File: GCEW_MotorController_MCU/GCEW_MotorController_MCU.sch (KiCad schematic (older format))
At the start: 4 parts, among them J1 Conn_02x03_Odd_Even, U1 ATMEGA328PB-AU

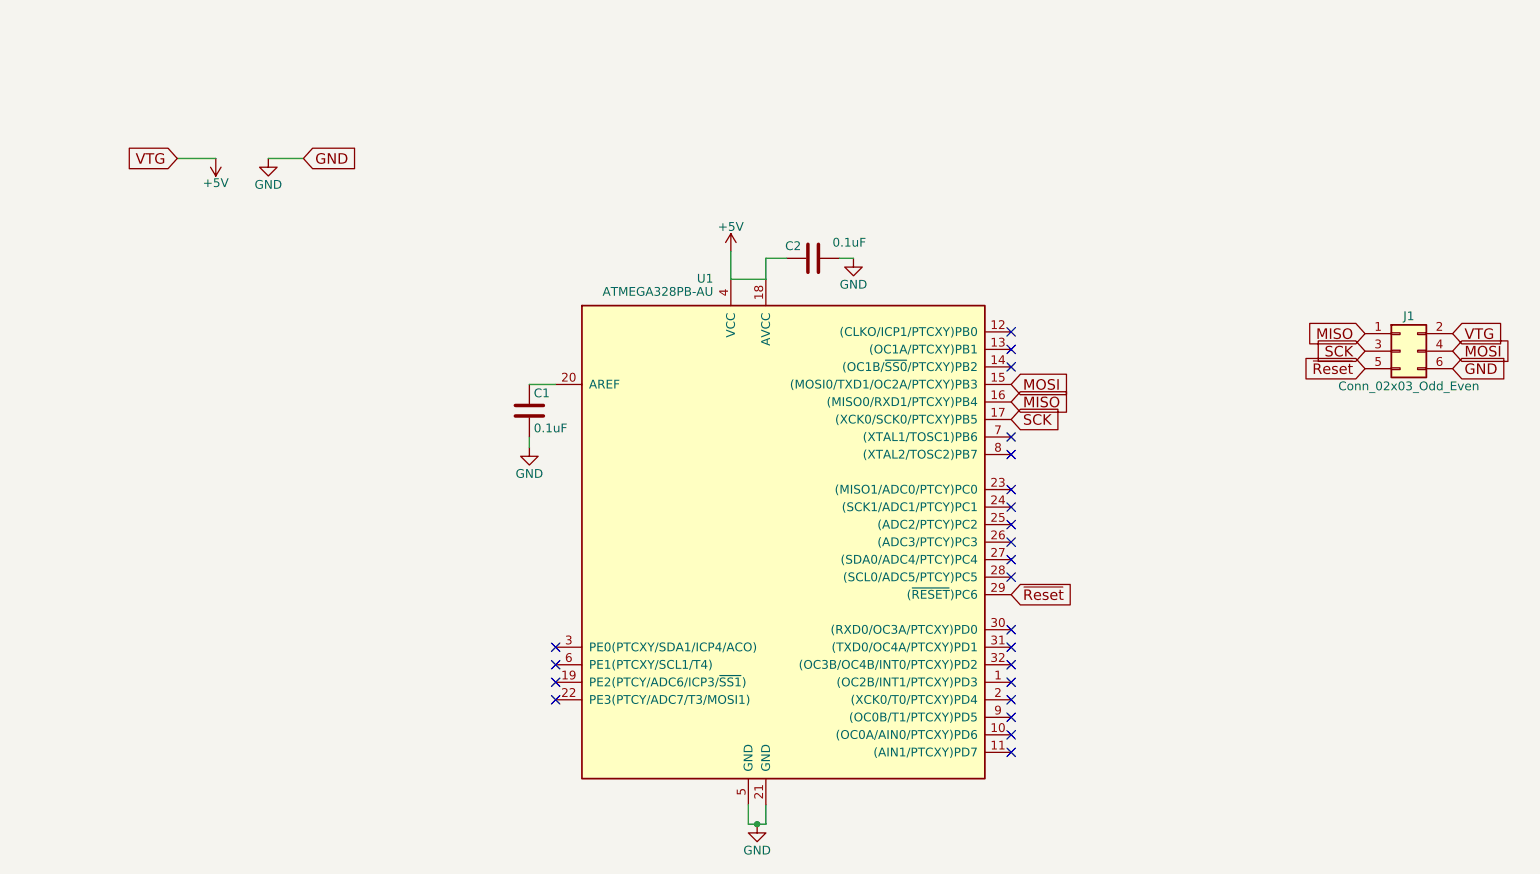
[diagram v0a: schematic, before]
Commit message: KiCAD Motor Controller MCU Schematic Update 1
Began KiCAD Schematic Design of Motor Controller MCU Board
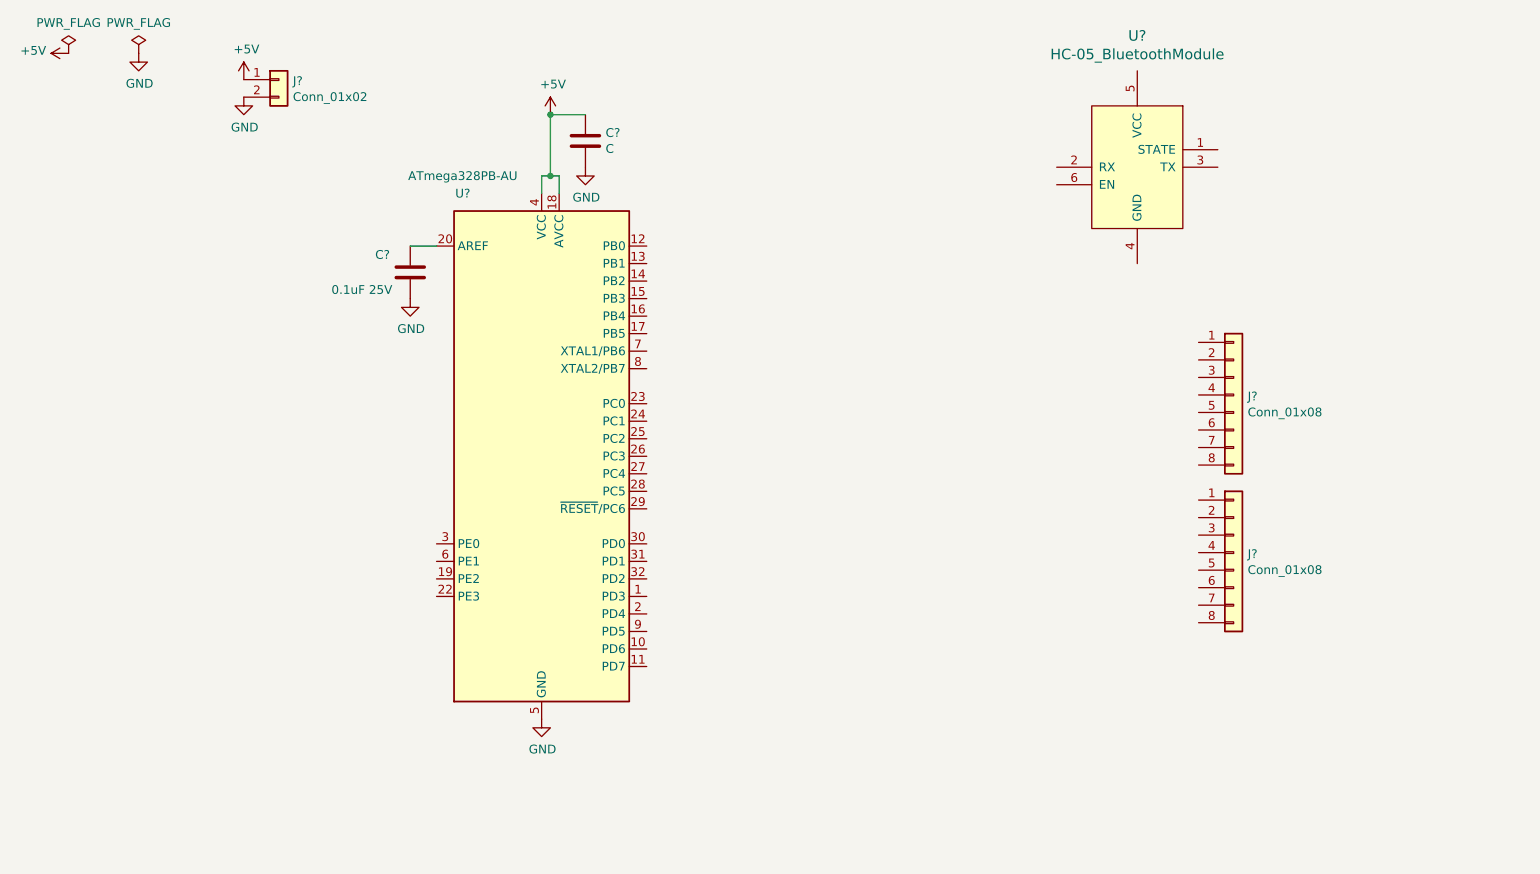
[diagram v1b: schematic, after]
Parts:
- removed C1, C2: 0.1uF, symbol C
- removed J1: Conn_02x03_Odd_Even, symbol Conn_02x03_Odd_Even
- removed U1: ATMEGA328PB-AU, Housings_QFP:TQFP-32_7x7mm_Pitch0.8mm, symbol ATMEGA328PB-AU
- added C?: C, symbol Device:C
- added C?: 0.1uF 25V, symbol Device:C
- added J? (x2): Conn_01x08, symbol Connector_Generic:Conn_01x08
- added J?: Conn_01x02, symbol Connector_Generic:Conn_01x02
- added U?: ATmega328PB-AU, Package_QFP:TQFP-32_7x7mm_P0.8mm, symbol MCU_Microchip_ATmega:ATmega328PB-AU
- added U?: HC-05_BluetoothModule, symbol myLib:HC-05_BluetoothModule
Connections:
- net +5V: now also C?.1, J?.1 (Pin_1), U?.18 (AVCC), U?.4 (VCC)
- net GND: now also C?.2, C?.2, J?.2 (Pin_2), U?.21 (GND), U?.5 (GND)
- new net: C?.1, U?.20 (AREF)
- no-connect marks 23 -> 0
